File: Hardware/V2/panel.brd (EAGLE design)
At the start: 99.8 x 99.8 mm, 122 parts, among them Q1 IRF3205STRLPBF, Q2 IRF3205STRLPBF, Q3 IRF3205STRLPBF, Q4 IRF3205STRLPBF, Q5 IRF3205STRLPBF, Q6 IRF3205STRLPBF, Q7 IRF3205STRLPBF, Q8 IRF3205STRLPBF, SW1 PTR1TP20R, U1 Value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

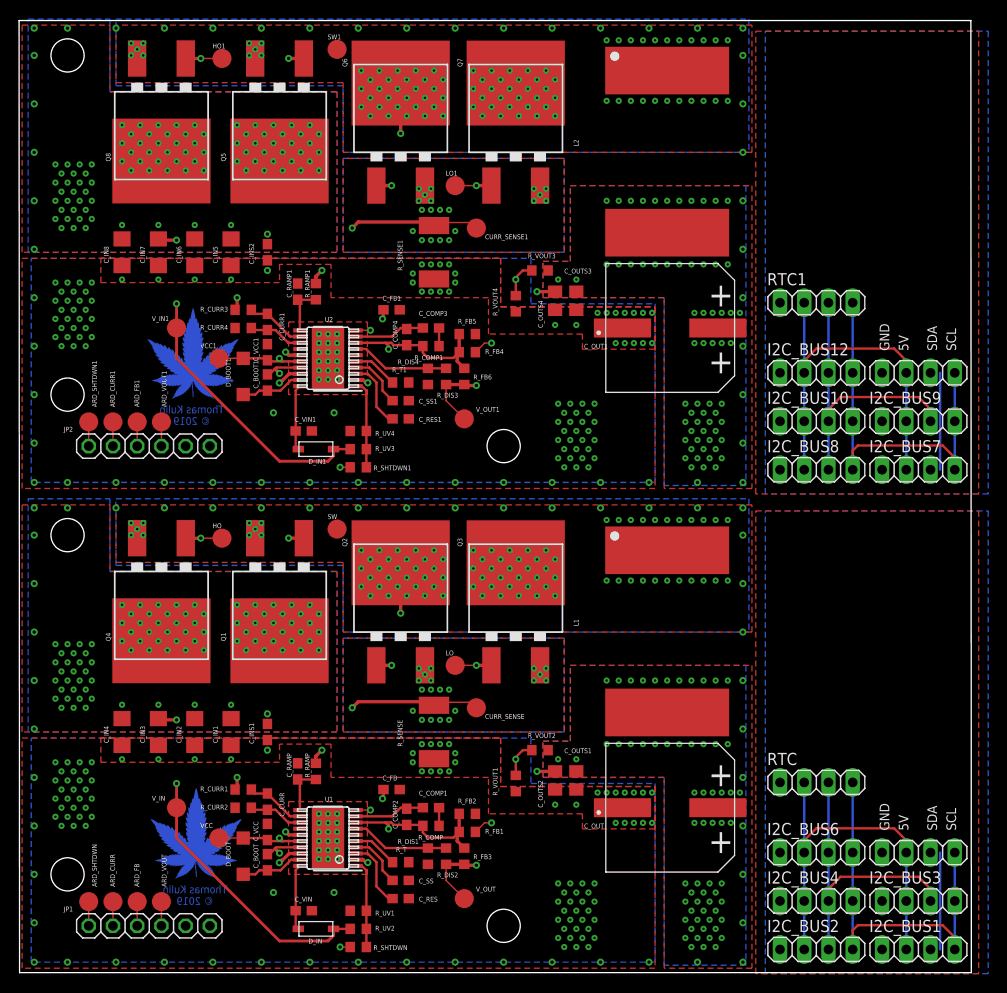
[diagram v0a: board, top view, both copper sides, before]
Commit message: updated buck v2.1 to reflect actual boards ordered from JLC
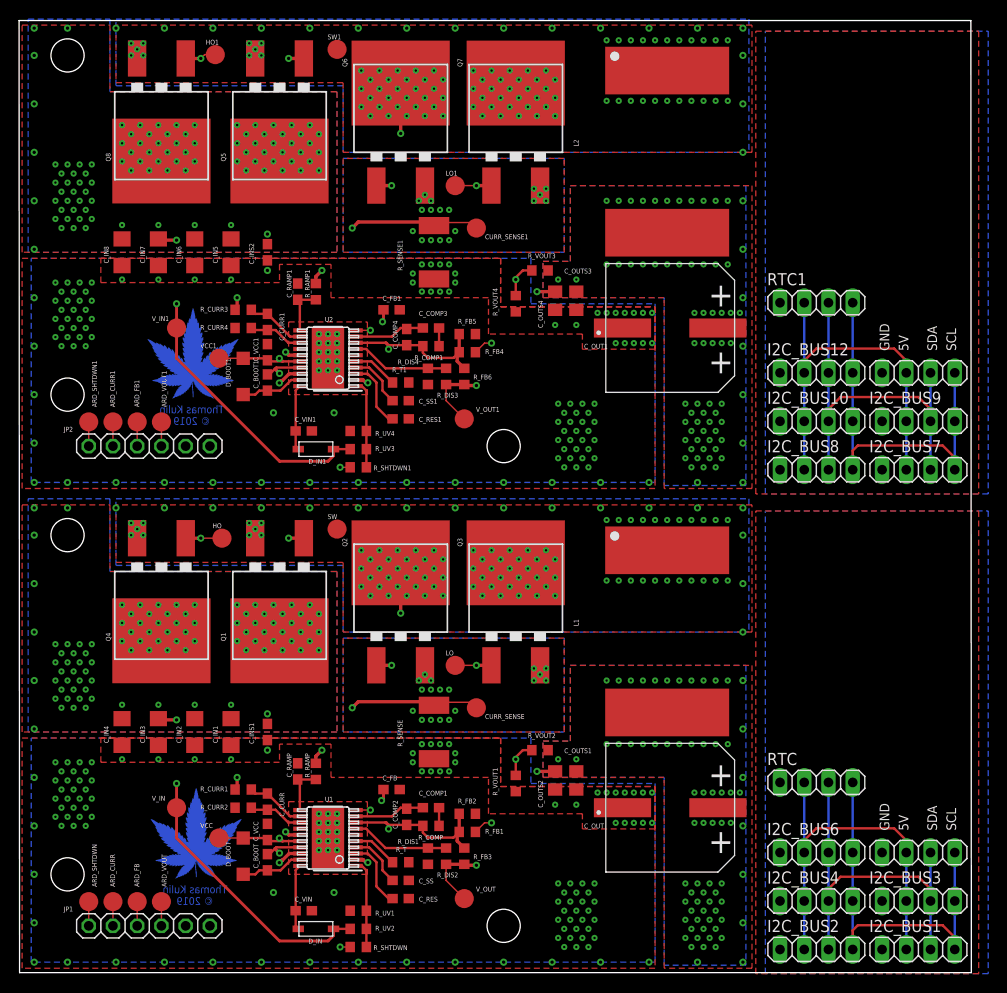
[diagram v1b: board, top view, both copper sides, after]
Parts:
- moved HO1 0.81 mm to (20.6, 96.3)
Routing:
- net N$4: vias 22 -> 20
- net N$38: vias 95 -> 92
- net N$23: vias 22 -> 20
- net N$21: vias 95 -> 92
